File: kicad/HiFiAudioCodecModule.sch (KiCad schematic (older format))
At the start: 26 parts, among them P1 CONN_01X06, P2 CONN_01X06, P3 CONN_02X05, U1 AK4558EN

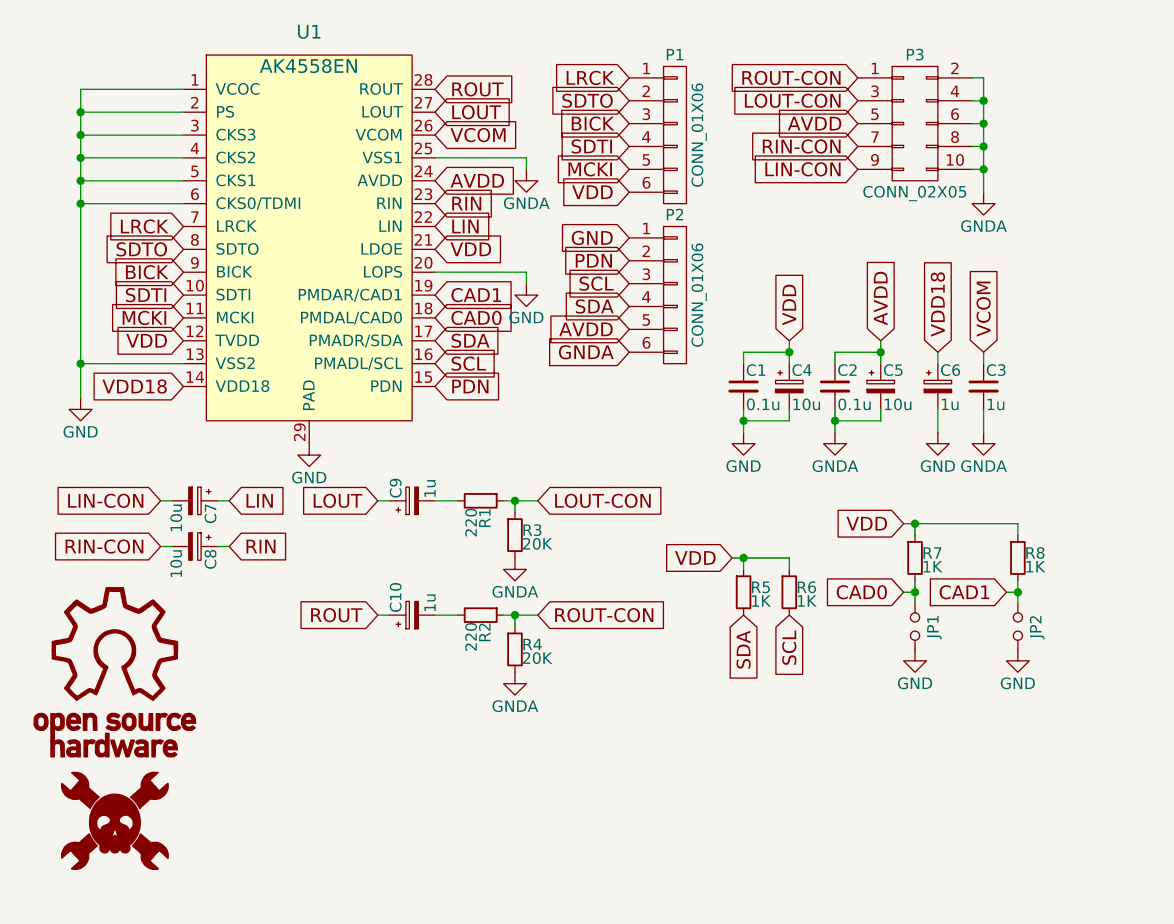
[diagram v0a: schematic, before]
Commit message: Added manf#s in schematic, fixed footprints, preparing rev.2
Preparing rev.2 layout:
-added manf# to check prices for manufacture w/ KiCost
-changed in/out decoupling caps to thru-hole bipolar audio caps
(Nichicon)
-reduced real estate requirements for bypass caps (all 3 mm dia. caps)

NOTE:LAYOUT COMPROMISED, STILL NEEDS TO BE FIXED
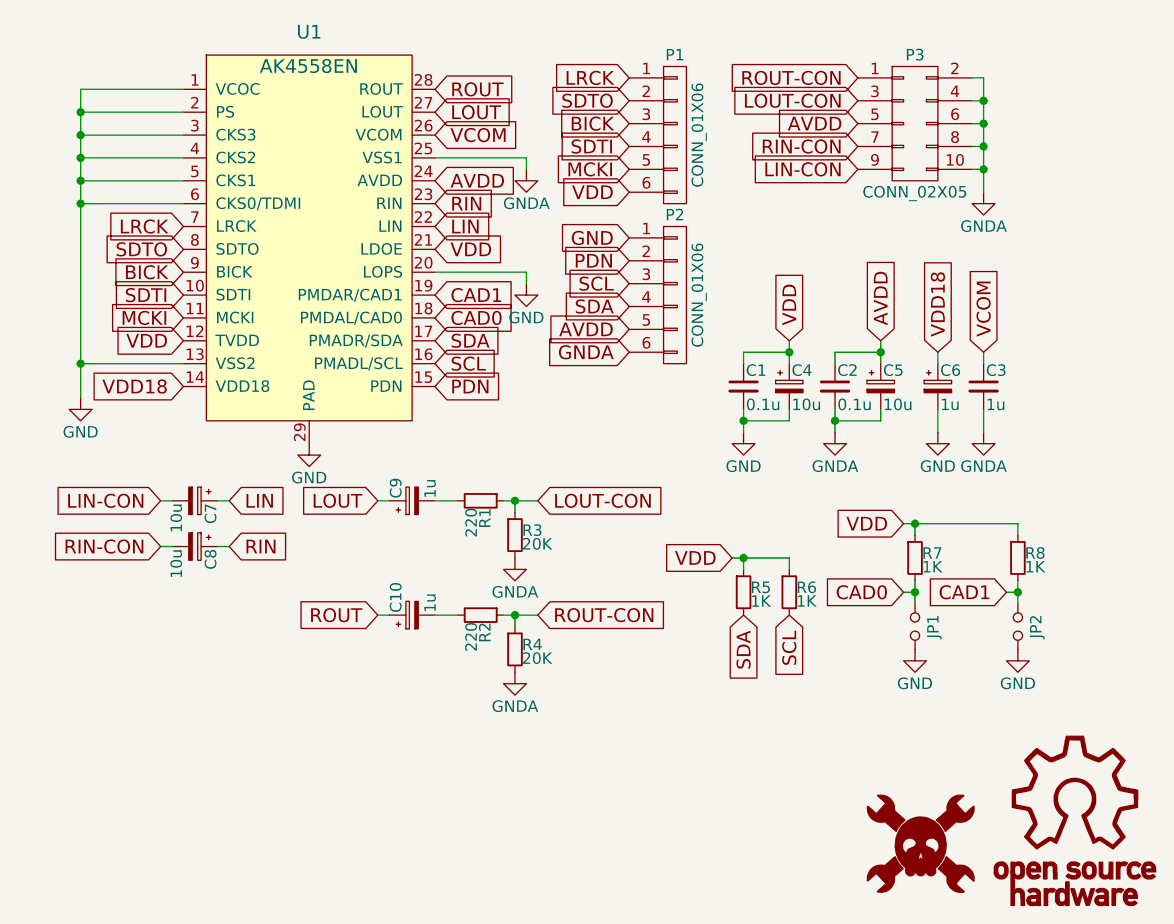
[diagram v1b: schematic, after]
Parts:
- C1, C2: footprint Capacitors_SMD:C_0402 -> HiFiAudioCodecModule-footprints:C_0402; manf# (none) -> CC0402KRX7R7BB104
- C10, C9: footprint Capacitors_SMD:c_elec_3x5.3 -> HiFiAudioCodecModule-footprints:C_Radial_D5_L11_P2-bipolar; manf# (none) -> UES1H010MDM1TD
- C3: footprint Capacitors_SMD:C_0402 -> HiFiAudioCodecModule-footprints:C_0402; manf# (none) -> CC0402KRX7R5BB105
- C4, C5: footprint Capacitors_SMD:c_elec_4x5.3 -> HiFiAudioCodecModule-footprints:CAP_ELEC_SMD_3x5mm; manf# (none) -> UWX1C100MCL2GB
- C6: footprint Capacitors_SMD:c_elec_3x5.3 -> HiFiAudioCodecModule-footprints:CAP_ELEC_SMD_3x5mm; manf# (none) -> UWX1C100MCL2GB
- C7, C8: footprint Capacitors_SMD:c_elec_4x5.3 -> HiFiAudioCodecModule-footprints:C_Radial_D5_L11_P2-bipolar; manf# (none) -> UES1E100MDM1TD
- JP1, JP2: footprint open-project:S_JUMPER_2 -> HiFiAudioCodecModule-footprints:SMD_Jumper
- P1, P2: footprint Pin_Headers:Pin_Header_Straight_1x06 -> HiFiAudioCodecModule-footprints:Pin_Header_Straight_1x06; manf# (none) -> M20-9990645
- P3: footprint Housings_DFN_QFN:Pin_Header_Straight_2x05_mod -> HiFiAudioCodecModule-footprints:Pin_Header_Straight_2x05; manf# (none) -> M20-9980545
- R1, R2: footprint Resistors_SMD:R_0402 -> HiFiAudioCodecModule-footprints:R_0402; manf# (none) -> RC0402FR-07220RL
- R3, R4: footprint Resistors_SMD:R_0402 -> HiFiAudioCodecModule-footprints:R_0402; manf# (none) -> RC0402FR-0720KL
- R5, R6, R7, R8: footprint Resistors_SMD:R_0402 -> HiFiAudioCodecModule-footprints:R_0402; manf# (none) -> RC0402FR-071KL
- U1: footprint Housings_DFN_QFN:QFN-28-2xEP_5x5mm_Pitch0.5mm -> HiFiAudioCodecModule-footprints:QFN-28-2xEP_5x5mm_Pitch0.5mm; manf# (none) -> AK4558EN
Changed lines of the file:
@@
 F 0 "U1" H 1700 2250 60  0000 C CNN
 F 1 "AK4558EN" H 1700 2100 60  0000 C CNN
-F 2 "Housings_DFN_QFN:QFN-28-2xEP_5x5mm_Pitch0.5mm" H 1400 2050 60  0001 C CNN
+F 2 "HiFiAudioCodecModule-footprints:QFN-28-2xEP_5x5mm_Pitch0.5mm" H 1400 2050 60  0001 C CNN
 F 3 "" H 1400 2050 60  0000 C CNN
+F 4 "AK4558EN" H 1700 1400 60  0001 C CNN "manf#"
 	1    1700 1400
 	1    0    0    -1
@@
 F 0 "C1" H 3610 2170 50  0000 L CNN
 F 1 "0.1u" H 3610 2020 50  0000 L CNN
-F 2 "Capacitors_SMD:C_0402" H 3600 2100 60  0001 C CNN
+F 2 "HiFiAudioCodecModule-footprints:C_0402" H 3600 2100 60  0001 C CNN
 F 3 "" H 3600 2100 60  0000 C CNN
+F 4 "CC0402KRX7R7BB104" H 3600 2100 60  0001 C CNN "manf#"
 	1    3600 2100
 	1    0    0    -1
@@
 F 0 "C4" H 3810 2170 50  0000 L CNN
 F 1 "10u" H 3810 2020 50  0000 L CNN
-F 2 "Capacitors_SMD:c_elec_4x5.3" H 3800 2100 60  0001 C CNN
+F 2 "HiFiAudioCodecModule-footprints:CAP_ELEC_SMD_3x5mm" H 3800 2100 60  0001 C CNN
 F 3 "" H 3800 2100 60  0000 C CNN
+F 4 "UWX1C100MCL2GB" H 3800 2100 60  0001 C CNN "manf#"
 	1    3800 2100
 	1    0    0    -1
@@
 F 0 "R1" H 2480 2620 50  0000 L CNN
 F 1 "220" H 2480 2560 50  0000 L CNN
-F 2 "Resistors_SMD:R_0402" H 2450 2600 60  0001 C CNN
+F 2 "HiFiAudioCodecModule-footprints:R_0402" H 2450 2600 60  0001 C CNN
 F 3 "" H 2450 2600 60  0000 C CNN
+F 4 "RC0402FR-07220RL" H 2450 2600 60  0001 C CNN "manf#"
 	1    2450 2600
 	0    1    1    0
@@
 F 0 "C2" H 4010 2170 50  0000 L CNN
 F 1 "0.1u" H 4010 2020 50  0000 L CNN
-F 2 "Capacitors_SMD:C_0402" H 4000 2100 60  0001 C CNN
+F 2 "HiFiAudioCodecModule-footprints:C_0402" H 4000 2100 60  0001 C CNN
 F 3 "" H 4000 2100 60  0000 C CNN
+F 4 "CC0402KRX7R7BB104" H 4000 2100 60  0001 C CNN "manf#"
 	1    4000 2100
 	1    0    0    -1
@@
 F 0 "C5" H 4210 2170 50  0000 L CNN
 F 1 "10u" H 4210 2020 50  0000 L CNN
-F 2 "Capacitors_SMD:c_elec_4x5.3" H 4200 2100 60  0001 C CNN
+F 2 "HiFiAudioCodecModule-footprints:CAP_ELEC_SMD_3x5mm" H 4200 2100 60  0001 C CNN
 F 3 "" H 4200 2100 60  0000 C CNN
+F 4 "UWX1C100MCL2GB" H 4200 2100 60  0001 C CNN "manf#"
 	1    4200 2100
 	1    0    0    -1
@@
 F 0 "C6" H 4460 2170 50  0000 L CNN
 F 1 "1u" H 4460 2020 50  0000 L CNN
-F 2 "Capacitors_SMD:c_elec_3x5.3" H 4450 2100 60  0001 C CNN
+F 2 "HiFiAudioCodecModule-footprints:CAP_ELEC_SMD_3x5mm" H 4450 2100 60  0001 C CNN
 F 3 "" H 4450 2100 60  0000 C CNN
+F 4 "UWX1C100MCL2GB" H 4450 2100 60  0001 C CNN "manf#"
 	1    4450 2100
 	1    0    0    -1
@@
 F 0 "C7" H 1210 2670 50  0000 L CNN
 F 1 "10u" H 1210 2520 50  0000 L CNN
-F 2 "Capacitors_SMD:c_elec_4x5.3" H 1200 2600 60  0001 C CNN
+F 2 "HiFiAudioCodecModule-footprints:C_Radial_D5_L11_P2-bipolar" H 1200 2600 60  0001 C CNN
 F 3 "" H 1200 2600 60  0000 C CNN
+F 4 "UES1E100MDM1TD" H 1200 2600 60  0001 C CNN "manf#"
 	1    1200 2600
 	0    1    1    0
@@
 F 0 "C8" H 1210 2870 50  0000 L CNN
 F 1 "10u" H 1210 2720 50  0000 L CNN
-F 2 "Capacitors_SMD:c_elec_4x5.3" H 1200 2800 60  0001 C CNN
+F 2 "HiFiAudioCodecModule-footprints:C_Radial_D5_L11_P2-bipolar" H 1200 2800 60  0001 C CNN
 F 3 "" H 1200 2800 60  0000 C CNN
+F 4 "UES1E100MDM1TD" H 1200 2800 60  0001 C CNN "manf#"
 	1    1200 2800
 	0    1    1    0
@@
 F 0 "C9" H 2160 2670 50  0000 L CNN
 F 1 "1u" H 2160 2520 50  0000 L CNN
-F 2 "Capacitors_SMD:c_elec_3x5.3" H 2150 2600 60  0001 C CNN
+F 2 "HiFiAudioCodecModule-footprints:C_Radial_D5_L11_P2-bipolar" H 2150 2600 60  0001 C CNN
 F 3 "" H 2150 2600 60  0000 C CNN
+F 4 "UES1H010MDM1TD" H 2150 2600 60  0001 C CNN "manf#"
 	1    2150 2600
 	0    -1   -1   0
@@
 F 0 "C10" H 2160 3170 50  0000 L CNN
 F 1 "1u" H 2160 3020 50  0000 L CNN
-F 2 "Capacitors_SMD:c_elec_3x5.3" H 2150 3100 60  0001 C CNN
+F 2 "HiFiAudioCodecModule-footprints:C_Radial_D5_L11_P2-bipolar" H 2150 3100 60  0001 C CNN
 F 3 "" H 2150 3100 60  0000 C CNN
+F 4 "UES1H010MDM1TD" H 2150 3100 60  0001 C CNN "manf#"
 	1    2150 3100
 	0    -1   -1   0
@@
 F 0 "C3" H 4660 2170 50  0000 L CNN
 F 1 "1u" H 4660 2020 50  0000 L CNN
-F 2 "Capacitors_SMD:C_0402" H 4650 2100 60  0001 C CNN
+F 2 "HiFiAudioCodecModule-footprints:C_0402" H 4650 2100 60  0001 C CNN
 F 3 "" H 4650 2100 60  0000 C CNN
+F 4 "CC0402KRX7R5BB105" H 4650 2100 60  0001 C CNN "manf#"
 	1    4650 2100
 	1    0    0    -1
@@
 F 0 "R2" H 2480 3120 50  0000 L CNN
 F 1 "220" H 2480 3060 50  0000 L CNN
-F 2 "Resistors_SMD:R_0402" H 2450 3100 60  0001 C CNN
+F 2 "HiFiAudioCodecModule-footprints:R_0402" H 2450 3100 60  0001 C CNN
 F 3 "" H 2450 3100 60  0000 C CNN
+F 4 "RC0402FR-07220RL" H 2450 3100 60  0001 C CNN "manf#"
 	1    2450 3100
 	0    1    1    0
@@
 F 0 "R3" H 2630 2770 50  0000 L CNN
 F 1 "20K" H 2630 2710 50  0000 L CNN
-F 2 "Resistors_SMD:R_0402" H 2600 2750 60  0001 C CNN
+F 2 "HiFiAudioCodecModule-footprints:R_0402" H 2600 2750 60  0001 C CNN
 F 3 "" H 2600 2750 60  0000 C CNN
+F 4 "RC0402FR-0720KL" H 2600 2750 60  0001 C CNN "manf#"
 	1    2600 2750
 	1    0    0    -1
@@
 F 0 "R4" H 2630 3270 50  0000 L CNN
 F 1 "20K" H 2630 3210 50  0000 L CNN
-F 2 "Resistors_SMD:R_0402" H 2600 3250 60  0001 C CNN
+F 2 "HiFiAudioCodecModule-footprints:R_0402" H 2600 3250 60  0001 C CNN
 F 3 "" H 2600 3250 60  0000 C CNN
+F 4 "RC0402FR-0720KL" H 2600 3250 60  0001 C CNN "manf#"
 	1    2600 3250
 	1    0    0    -1
@@
 F 0 "R5" H 3630 3020 50  0000 L CNN
 F 1 "1K" H 3630 2960 50  0000 L CNN
-F 2 "Resistors_SMD:R_0402" H 3600 3000 60  0001 C CNN
+F 2 "HiFiAudioCodecModule-footprints:R_0402" H 3600 3000 60  0001 C CNN
 F 3 "" H 3600 3000 60  0000 C CNN
+F 4 "RC0402FR-071KL" H 3600 3000 60  0001 C CNN "manf#"
 	1    3600 3000
 	1    0    0    -1
@@
 F 0 "R6" H 3830 3020 50  0000 L CNN
 F 1 "1K" H 3830 2960 50  0000 L CNN
-F 2 "Resistors_SMD:R_0402" H 3800 3000 60  0001 C CNN
+F 2 "HiFiAudioCodecModule-footprints:R_0402" H 3800 3000 60  0001 C CNN
 F 3 "" H 3800 3000 60  0000 C CNN
+F 4 "RC0402FR-071KL" H 3800 3000 60  0001 C CNN "manf#"
 	1    3800 3000
 	1    0    0    -1
@@
 F 0 "JP1" H 4350 3230 50  0000 C CNN
 F 1 "Jumper_NO_Small" H 4360 3090 50  0001 C CNN
-F 2 "open-project:S_JUMPER_2" H 4350 3150 60  0001 C CNN
+F 2 "HiFiAudioCodecModule-footprints:SMD_Jumper" H 4350 3150 60  0001 C CNN
 F 3 "" H 4350 3150 60  0000 C CNN
 	1    4350 3150
@@
 F 0 "R7" H 4380 2870 50  0000 L CNN
 F 1 "1K" H 4380 2810 50  0000 L CNN
-F 2 "Resistors_SMD:R_0402" H 4350 2850 60  0001 C CNN
+F 2 "HiFiAudioCodecModule-footprints:R_0402" H 4350 2850 60  0001 C CNN
 F 3 "" H 4350 2850 60  0000 C CNN
+F 4 "RC0402FR-071KL" H 4350 2850 60  0001 C CNN "manf#"
 	1    4350 2850
 	1    0    0    -1
@@
 F 0 "R8" H 4830 2870 50  0000 L CNN
 F 1 "1K" H 4830 2810 50  0000 L CNN
-F 2 "Resistors_SMD:R_0402" H 4800 2850 60  0001 C CNN
+F 2 "HiFiAudioCodecModule-footprints:R_0402" H 4800 2850 60  0001 C CNN
 F 3 "" H 4800 2850 60  0000 C CNN
+F 4 "RC0402FR-071KL" H 4800 2850 60  0001 C CNN "manf#"
 	1    4800 2850
 	1    0    0    -1
@@
 F 0 "JP2" H 4800 3230 50  0000 C CNN
 F 1 "Jumper_NO_Small" H 4810 3090 50  0001 C CNN
-F 2 "open-project:S_JUMPER_2" H 4800 3150 60  0001 C CNN
+F 2 "HiFiAudioCodecModule-footprints:SMD_Jumper" H 4800 3150 60  0001 C CNN
 F 3 "" H 4800 3150 60  0000 C CNN
 	1    4800 3150
@@
 F 0 "P1" H 3300 1350 50  0000 C CNN
 F 1 "CONN_01X06" V 3400 1000 50  0000 C CNN
-F 2 "Pin_Headers:Pin_Header_Straight_1x06" H 3300 1000 60  0001 C CNN
+F 2 "HiFiAudioCodecModule-footprints:Pin_Header_Straight_1x06" H 3300 1000 60  0001 C CNN
 F 3 "" H 3300 1000 60  0000 C CNN
+F 4 "M20-9990645" H 3300 1000 60  0001 C CNN "manf#"
 	1    3300 1000
 	1    0    0    -1
@@
 F 0 "P2" H 3300 2050 50  0000 C CNN
 F 1 "CONN_01X06" V 3400 1700 50  0000 C CNN
-F 2 "Pin_Headers:Pin_Header_Straight_1x06" H 3300 1700 60  0001 C CNN
+F 2 "HiFiAudioCodecModule-footprints:Pin_Header_Straight_1x06" H 3300 1700 60  0001 C CNN
 F 3 "" H 3300 1700 60  0000 C CNN
+F 4 "M20-9990645" H 3300 1700 60  0001 C CNN "manf#"
 	1    3300 1700
 	1    0    0    -1
@@
 F 0 "P3" H 4350 1250 50  0000 C CNN
 F 1 "CONN_02X05" H 4350 650 50  0000 C CNN
-F 2 "Housings_DFN_QFN:Pin_Header_Straight_2x05_mod" H 4350 -250 60  0001 C CNN
+F 2 "HiFiAudioCodecModule-footprints:Pin_Header_Straight_2x05" H 4350 -250 60  0001 C CNN
 F 3 "" H 4350 -250 60  0000 C CNN
+F 4 "M20-9980545" H 4350 950 60  0001 C CNN "manf#"
 	1    4350 950
 	1    0    0    -1
@@
 L HACKADAY LOGO2
 U 1 1 5667295B
-P 850 4000
-F 0 "LOGO2" H 850 3818 60  0001 C CNN
-F 1 "HACKADAY" H 850 4182 60  0001 C CNN
-F 2 "hackaday_logo:LOGO" H 850 4000 60  0001 C CNN
-F 3 "" H 850 4000 60  0000 C CNN
-	1    850  4000
+P 4375 4100
+F 0 "LOGO2" H 4375 3918 60  0001 C CNN
+F 1 "HACKADAY" H 4375 4282 60  0001 C CNN
+F 2 "hackaday_logo:LOGO" H 4375 4100 60  0001 C CNN
+F 3 "" H 4375 4100 60  0000 C CNN
+	1    4375 4100
 	1    0    0    -1
 $EndComp
@@
 L OSHW LOGO1
 U 1 1 5667299F
-P 850 3350
-F 0 "LOGO1" H 850 3010 60  0001 C CNN
-F 1 "OSHW" H 850 3690 60  0001 C CNN
-F 2 "oshw_logo:LOGO" H 850 3350 60  0001 C CNN
-F 3 "" H 850 3350 60  0000 C CNN
-	1    850  3350
-	1    0    0    -1
-$EndComp
+P 5050 4000
+F 0 "LOGO1" H 5050 3660 60  0001 C CNN
+F 1 "OSHW" H 5050 4340 60  0001 C CNN
+F 2 "oshw_logo:LOGO" H 5050 4000 60  0001 C CNN
+F 3 "" H 5050 4000 60  0000 C CNN
+	1    5050 4000
+	1    0    0    -1
+$EndComp
